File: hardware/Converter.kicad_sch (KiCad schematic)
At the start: 80 parts, among them J3 CON2, J4 CON2, J5 CON2, J7 CON2, Q1 SIR880BDP, Q2 SIR880BDP, Q3 SIR880BDP, Q4 SIR880BDP, U4 BQ25758

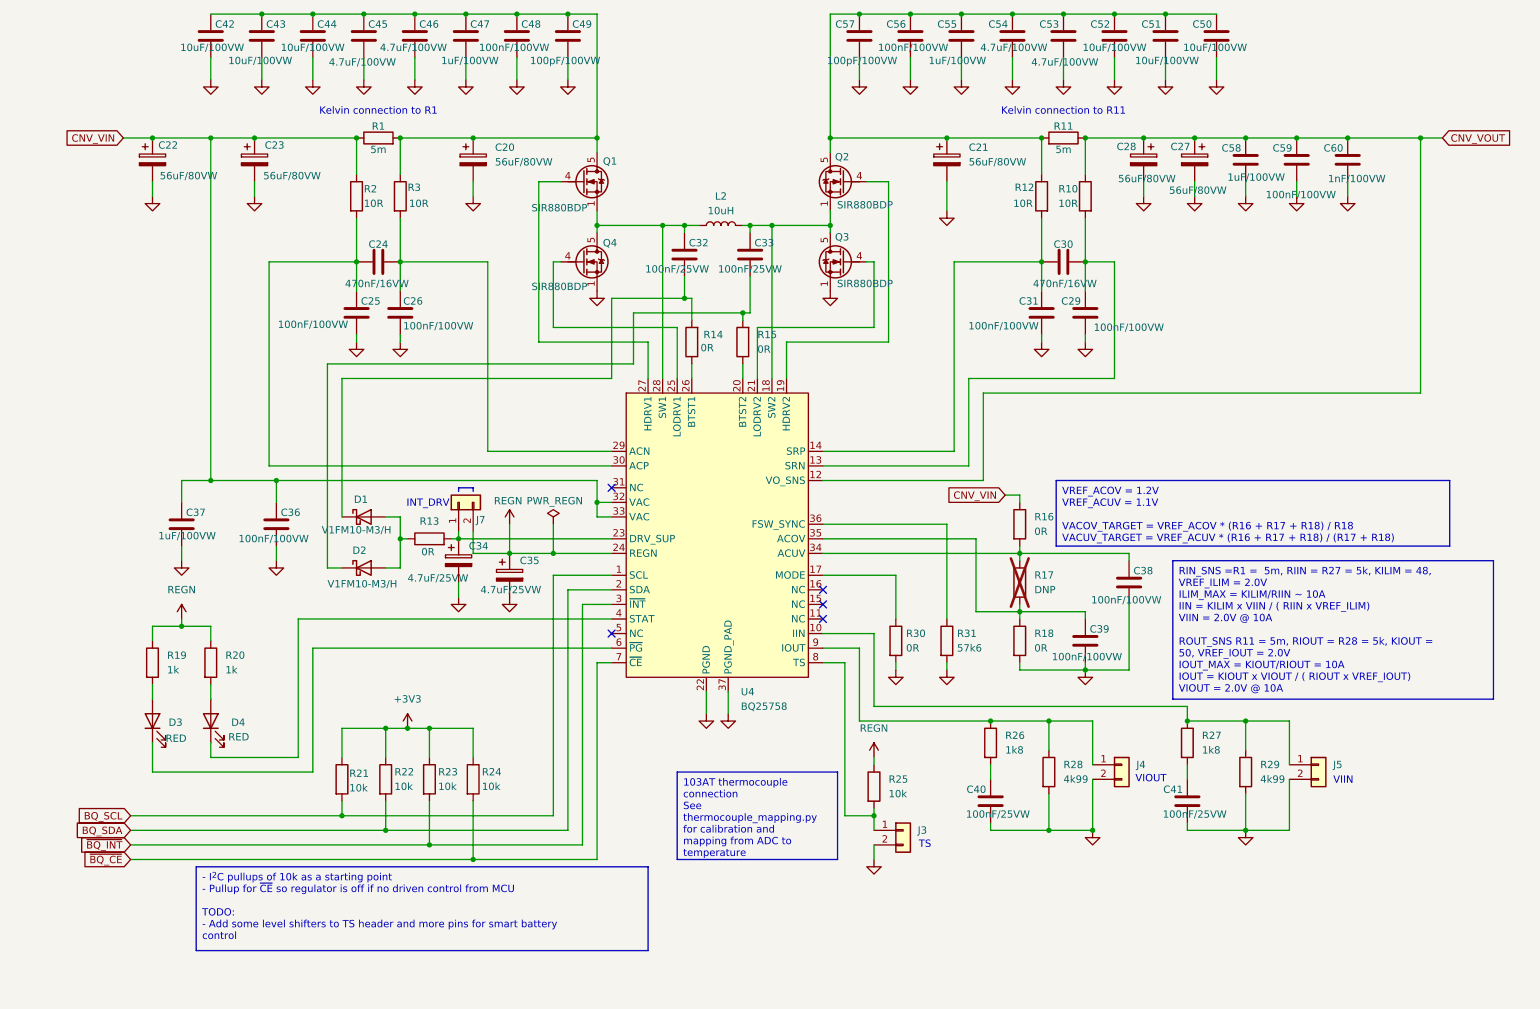
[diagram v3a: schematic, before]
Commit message: All components placed on board and most 3D shapes are present
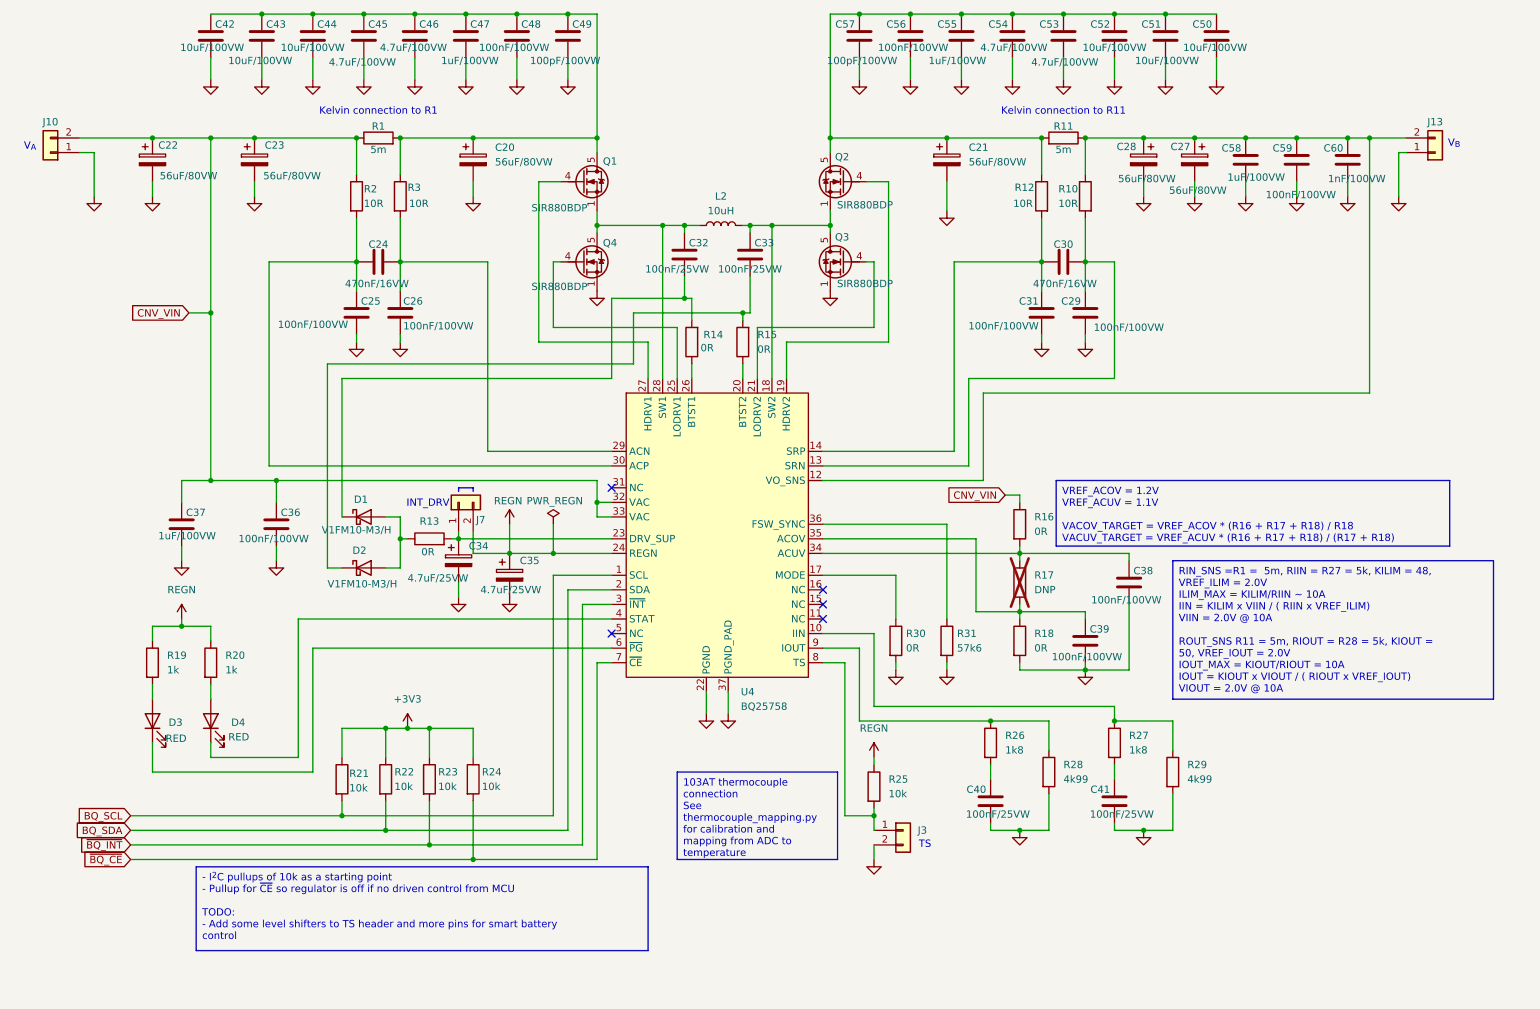
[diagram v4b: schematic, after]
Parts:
- removed J4, J5: CON2, Connector_PinHeader_2.54mm:PinHeader_1x02_P2.54mm_Vertical, symbol Connector_Generic:Conn_01x02
- added J10, J13: Conn_01x02, Connector_Phoenix_MSTB:PhoenixContact_MSTBVA_2,5_2-G-5,08_1x02_P5.08mm_Vertical, symbol Connector_Generic:Conn_01x02
- C42, C43, C44, C50, C51, C52: footprint Capacitor_SMD:CP_Elec_6.3x7.7 -> Capacitor_SMD:C_1206_3216Metric; JLCPCB C19077968 -> C5156756
- C45, C46, C53, C54: footprint Capacitor_SMD:CP_Elec_6.3x7.7 -> Capacitor_SMD:C_1210_3225Metric; JLCPCB C970653 -> C385986
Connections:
- net CNV_VIN: now also J10.2 (Pin_2)
- net GND: now also J10.1 (Pin_1), J13.1 (Pin_1)
- net CNV_VOUT: no longer names the net of C27.1, C28.1, C58.1, C59.1, C60.1, R10.1, R11.1, U4.12 (VO_SNS)
- net CNV_VOUT: now also J13.2 (Pin_2)
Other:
- note added: "V_{A}"
- note added: "V_{B}"
- note removed: "VIIN"
- note removed: "VIOUT"
- moved on the sheet: C41, R27, R29

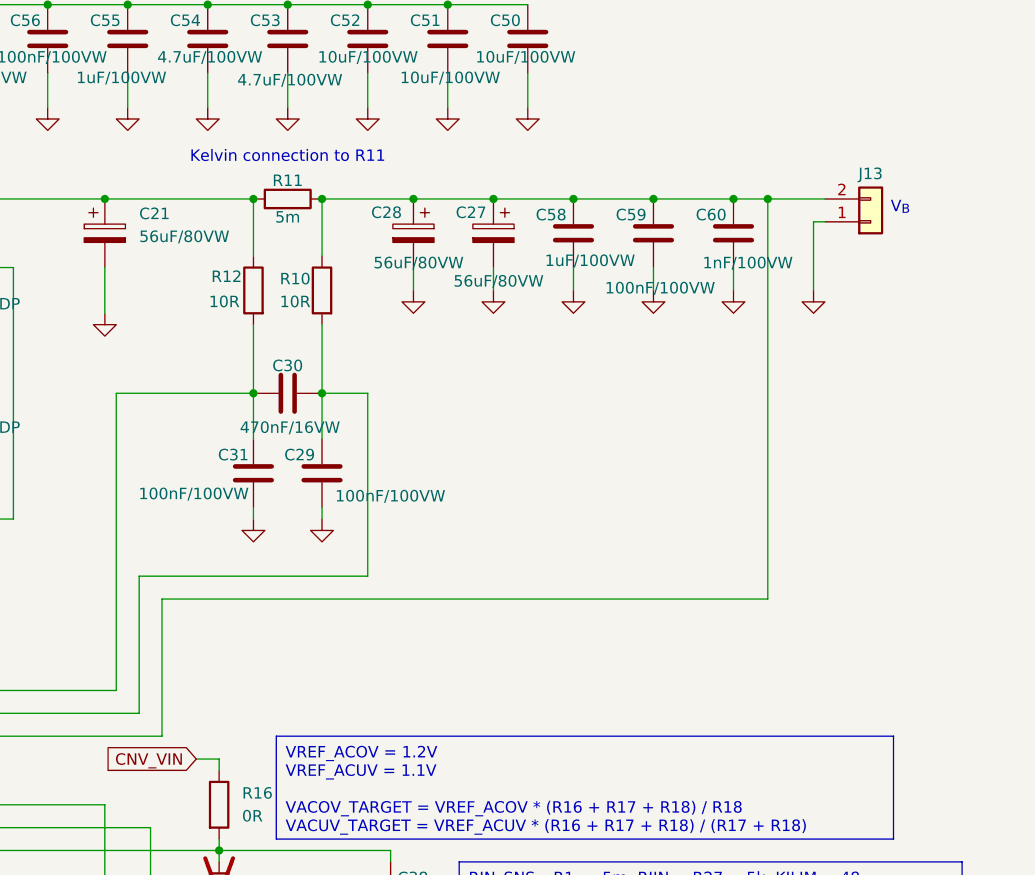
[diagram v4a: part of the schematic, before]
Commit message: - Routed board with all fixable DRC errors and warnings fixed
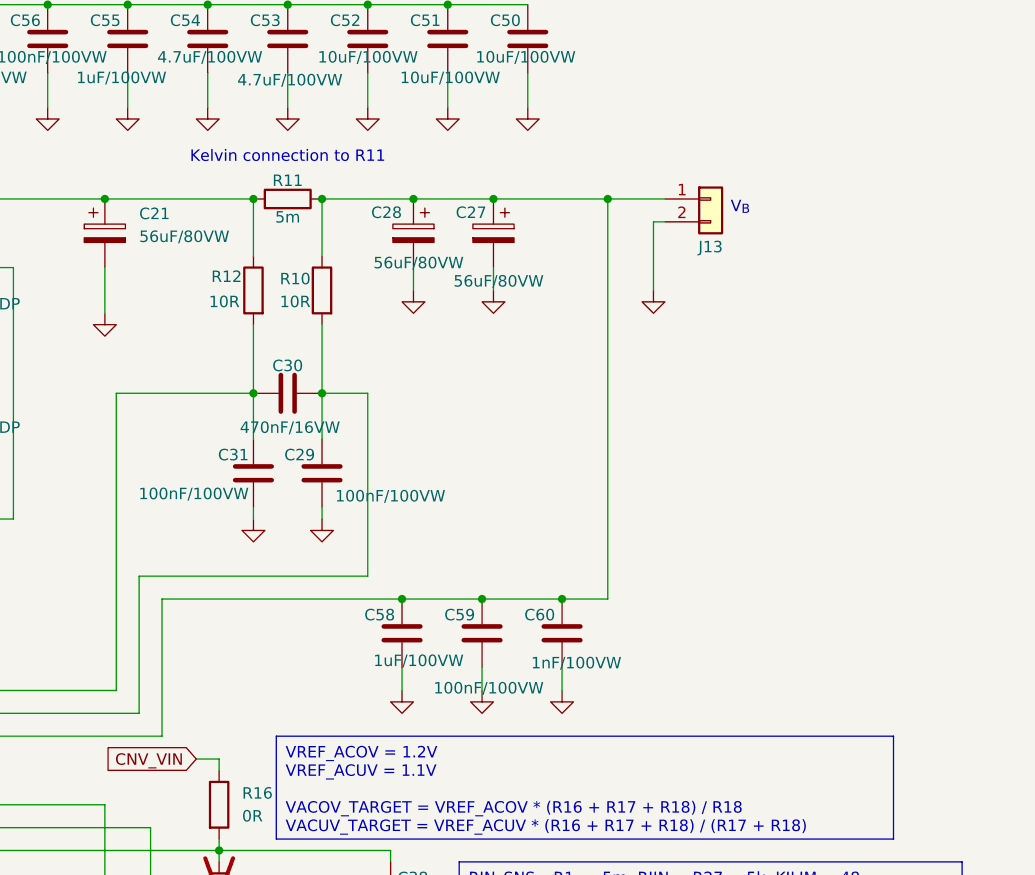
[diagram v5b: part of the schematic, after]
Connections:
- net GND: now also J13.2 (Pin_2); no longer J13.1 (Pin_1)
- net at C27.1, C28.1, C58.1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: now also J13.1 (Pin_1); no longer J13.2 (Pin_2)
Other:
- moved on the sheet: C58, C59, C60, J13

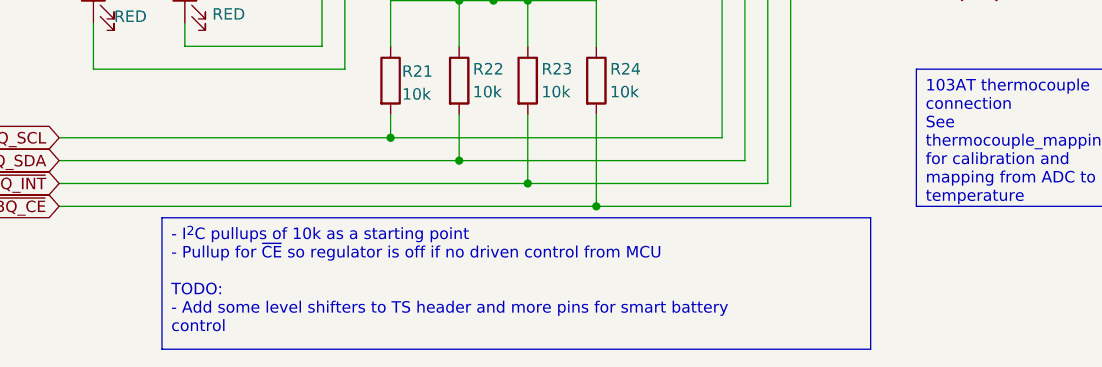
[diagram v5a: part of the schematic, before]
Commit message: Added summary page Added prototyping area to PCB
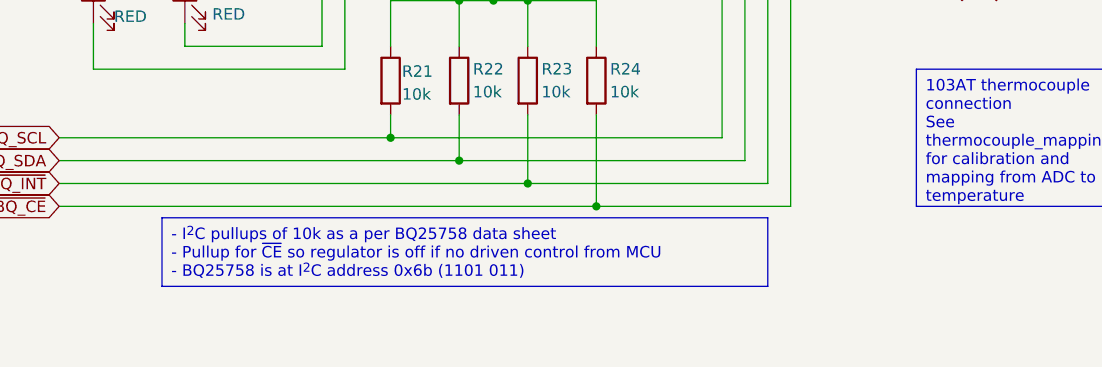
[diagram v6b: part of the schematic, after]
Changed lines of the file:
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@@
 		)
 	)
-	(text_box "- I^{2}C pullups of 10k as a starting point\n- Pullup for ~{CE} so regulator is off if no driven control from MCU\n\nTODO:\n- Add some level shifters to TS header and more pins for smart battery control"
+	(text_box "- I^{2}C pullups of 10k as a per BQ25758 data sheet\n- Pullup for ~{CE} so regulator is off if no driven control from MCU\n- BQ25758 is at I^{2}C address 0x6b (1101 011)"
 		(exclude_from_sim no)
 		(at 54.61 167.64 0)
-		(size 78.74 14.605)
+		(size 67.31 7.62)
 		(stroke
 			(width 0)

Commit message: Ready for trial submit to JLCPCB
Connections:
- net CNV_VIN: now also J10.1 (Pin_1); no longer J10.2 (Pin_2)
- net GND: now also J10.2 (Pin_2), J13.1 (Pin_1); no longer J10.1 (Pin_1), J13.2 (Pin_2)
- net at C27.1, C28.1, C58.1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: now also J13.2 (Pin_2); no longer J13.1 (Pin_1)
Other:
- moved on the sheet: J10

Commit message: * Added the JLCPCB Fabrication Plugin into KiCad and use this for the exports * Fixed problem detected with capacitor footprint for C42, C43, C44, C50, C51, C52
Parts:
- C20, C21, C22, C23, C27, C28: LCSC Part (none) -> C128515
- C24, C30: LCSC Part (none) -> C1623
- C25, C26, C29, C31, C36, C38, C39, C48, C56, C59: LCSC Part (none) -> C1945
- C32, C33, C40, C41: LCSC Part (none) -> C1590
- C34, C35: LCSC Part (none) -> C1779
- C37, C47, C55, C58: LCSC Part (none) -> C13832
- C42, C43, C44, C50, C51, C52: footprint Capacitor_SMD:C_1206_3216Metric -> Capacitor_SMD:C_1210_3225Metric; LCSC Part (none) -> C5156756
- C45, C46, C53, C54: LCSC Part (none) -> C385986
- C49, C57: LCSC Part (none) -> C37456
- C60: LCSC Part (none) -> C15177
- D1, D2: LCSC Part (none) -> C3758930
- D3, D4: LCSC Part (none) -> C2286
- R1, R11: LCSC Part (none) -> C481477
- R10, R12, R2, R3: LCSC Part (none) -> C22859
- R13, R14, R15, R16, R18, R30: LCSC Part (none) -> C21189
- R19, R20: LCSC Part (none) -> C21190
- R21, R22, R23, R24, R25: LCSC Part (none) -> C25804
- R26, R27: LCSC Part (none) -> C4177
- R28, R29: LCSC Part (none) -> C2692815
- R31: LCSC Part (none) -> C23082
- U4: LCSC Part (none) -> C33222334
